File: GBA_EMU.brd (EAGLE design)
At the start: 130.7 x 72.9 mm, 78 parts, among them IC1 MEGA16U2, J2 AUDIO-JACK2SMD, Q1 MOSFET-PCHANNEL, SW1 LEFT, SW2 RIGHT, SW3 PWR_SWITCH, SW4 R2, SW5 L2, U1 RPI-ZERO, U2 FT230X, U3 MCP1642B-ADJ, U4 LM4875, U5 V_REG_LDOSMD2, U6 MIC7221, U7 AZV321

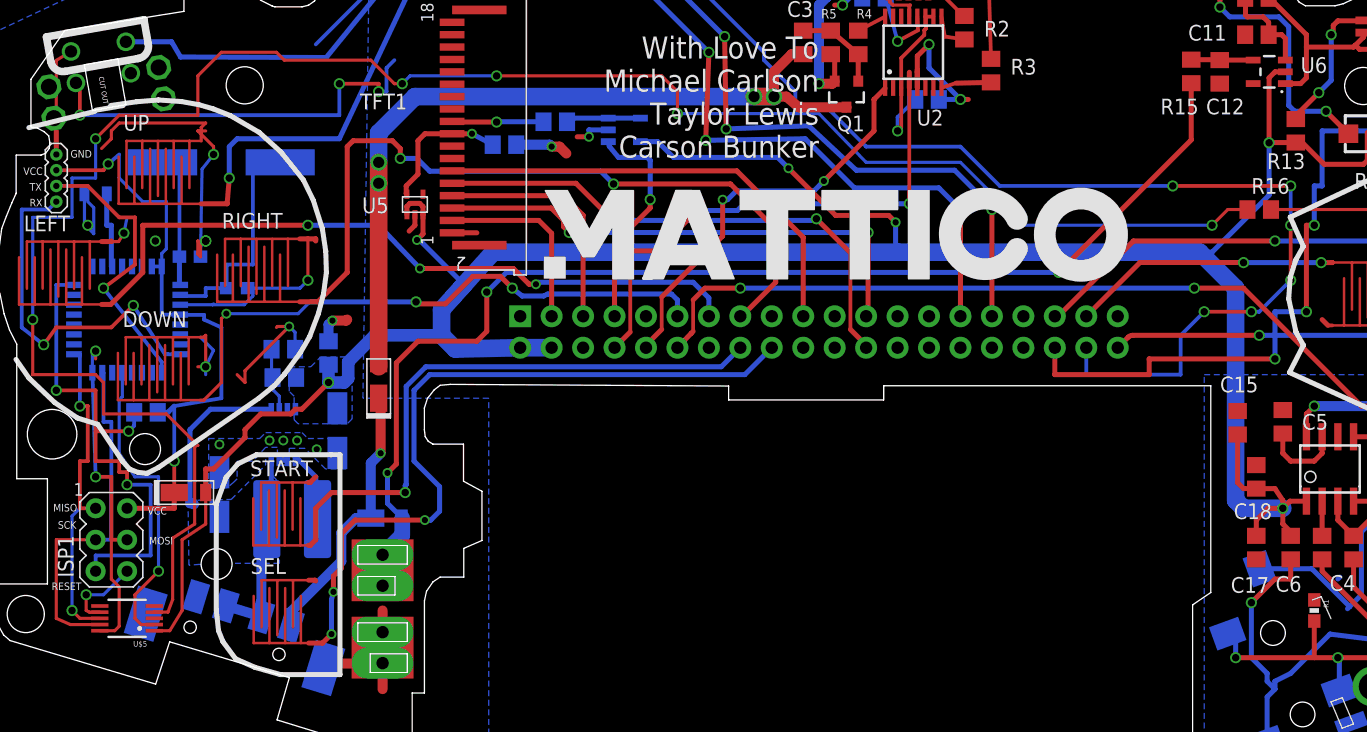
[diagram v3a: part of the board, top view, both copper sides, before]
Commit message: added soureable switch
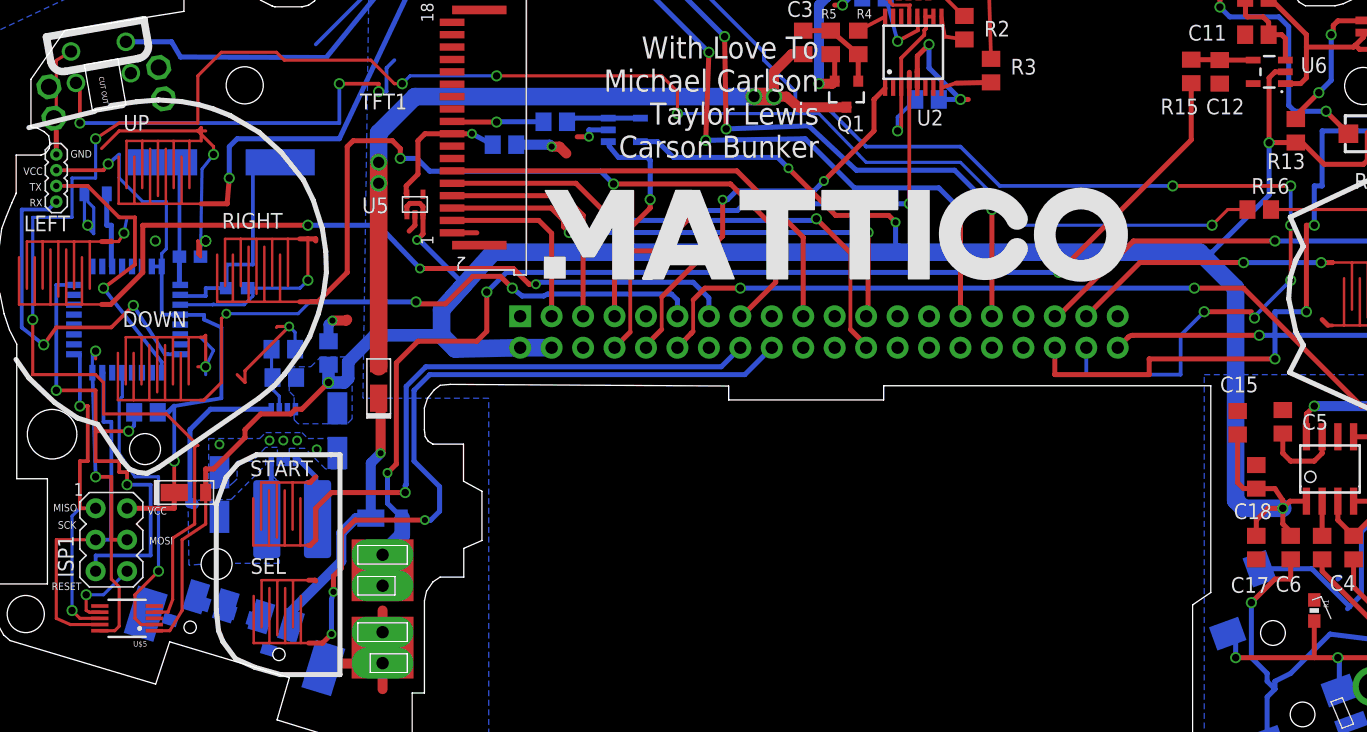
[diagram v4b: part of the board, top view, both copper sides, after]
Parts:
- added SW6: GBA_PWR_SWITCHJSX, custom:JSX08001SAQNL_SWITCH
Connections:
- new net N$13: SW3.1
- net 0.8128: no longer SW3.COM1, SW3.COM2
- net N$18: no longer SW3.1
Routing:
- net 0.8128: track 30.2 -> 22.2 mm
- net L2_BUMP: track 155.6 -> 157.5 mm
- net GND: track 178.2 -> 176.8 mm
- net N$18: track 22.1 -> 21.0 mm
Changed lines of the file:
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@@
 <attribute name="PROD_ID" value="RES-07871" x="127.635" y="23.495" size="1.778" layer="27" rot="R270" display="off"/>
 </element>
+<element name="SW6" library="custom" package="JSX08001SAQNL_SWITCH" value="GBA_PWR_SWITCHJSX" x="43.18" y="20.32" rot="MR17"/>
 </elements>
 <signals>
@@
 <contactref element="U$5" pad="7"/>
 <wire x1="37.737625" y1="61.42204375" x2="37.737625" y2="62.502625" width="0.254" layer="1"/>
-<wire x1="37.737625" y1="62.502625" x2="38.1" y2="62.865" width="0.254" layer="1"/>
-<wire x1="38.1" y1="62.865" x2="31.115" y2="62.865" width="0.254" layer="1"/>
+<wire x1="37.737625" y1="62.502625" x2="37.465" y2="62.23" width="0.254" layer="1"/>
+<wire x1="37.465" y1="62.23" x2="31.115" y2="62.23" width="0.254" layer="1"/>
 <wire x1="26.035" y1="62.23" x2="26.035" y2="67.92616875" width="0.254" layer="1"/>
 <wire x1="26.035" y1="67.92616875" x2="27.221940625" y2="68.644228125" width="0.254" layer="1"/>
@@
 <wire x1="38.735" y1="60.96" x2="37.465" y2="62.23" width="0.254" layer="1"/>
 <wire x1="37.465" y1="62.23" x2="38.1" y2="62.23" width="0.254" layer="1"/>
-<wire x1="29.69269375" y1="60.80769375" x2="30.48" y2="61.595" width="0.254" layer="1"/>
-<wire x1="30.48" y1="61.595" x2="30.48" y2="62.23" width="0.254" layer="1"/>
-<wire x1="30.48" y1="62.23" x2="31.115" y2="62.865" width="0.254" layer="1"/>
+<wire x1="29.69269375" y1="60.80769375" x2="31.115" y2="62.23" width="0.254" layer="1"/>
 <wire x1="29.55" y1="23.36" x2="28.71" y2="23.36" width="0.254" layer="1"/>
 <wire x1="28.71" y1="23.36" x2="28.448" y2="23.495" width="0.254" layer="1"/>
@@
 <wire x1="123.8262125" y1="12.886290625" x2="123.8262125" y2="16.5112125" width="0.4064" layer="16"/>
 <wire x1="123.8262125" y1="16.5112125" x2="124.46" y2="17.145" width="0.4064" layer="16"/>
-<wire x1="40.64" y1="42.545" x2="38.1" y2="42.545" width="0" layer="19" extent="1-16"/>
+<wire x1="42.61191875" y1="25.943271875" x2="31.75" y2="26.67" width="0" layer="19" extent="1-1"/>
+<wire x1="38.1" y1="42.545" x2="40.64" y2="42.545" width="0" layer="19" extent="1-16"/>
 <wire x1="96.52" y1="69.215" x2="94.925" y2="71.455" width="0" layer="19" extent="1-16"/>
-<wire x1="31.75" y1="26.67" x2="42.61191875" y2="25.943271875" width="0" layer="19" extent="1-1"/>
+<wire x1="128.740265625" y1="46.519734375" x2="125.095" y2="39.685" width="0" layer="19" extent="1-1"/>
 </signal>
 <signal name="TXD">
@@
 <wire x1="36.83" y1="38.1" x2="36.83" y2="32.146875" width="0.4064" layer="16"/>
 <wire x1="43.395625" y1="30.76125" x2="43.395625" y2="28.835625" width="0.8128" layer="16"/>
-<contactref element="SW3" pad="COM2"/>
-<contactref element="SW3" pad="COM1"/>
-<wire x1="42.59605625" y1="22.99866875" x2="42.59605625" y2="28.03605625" width="0.8128" layer="16"/>
 <wire x1="42.59605625" y1="28.03605625" x2="43.395625" y2="28.835625" width="0.8128" layer="16"/>
-<wire x1="42.59605625" y1="22.99866875" x2="39.727140625" y2="23.875784375" width="0.8128" layer="16"/>
 </signal>
 <signal name="N$20">
@@
 <wire x1="50.244375" y1="30.95625" x2="49.05375" y2="29.765625" width="0.8128" layer="16"/>
 <wire x1="49.05375" y1="29.765625" x2="49.05375" y2="27.46375" width="0.8128" layer="16"/>
-<contactref element="SW3" pad="1"/>
-<wire x1="44.986815625" y1="22.267740625" x2="44.986815625" y2="23.396815625" width="0.8128" layer="16"/>
 <wire x1="44.986815625" y1="23.396815625" x2="49.05375" y2="27.46375" width="0.8128" layer="16"/>
 </signal>
@@
 <wire x1="43.815" y1="68.58" x2="39.37" y2="68.58" width="0.254" layer="1"/>
 <wire x1="39.37" y1="68.58" x2="37.465" y2="66.675" width="0.254" layer="1"/>
-<wire x1="37.465" y1="66.675" x2="37.465" y2="63.5" width="0.254" layer="1"/>
-<wire x1="37.465" y1="63.5" x2="31.115" y2="63.5" width="0.254" layer="1"/>
-<wire x1="31.115" y1="63.5" x2="29.21" y2="61.595" width="0.254" layer="1"/>
+<wire x1="37.465" y1="66.675" x2="37.465" y2="62.865" width="0.254" layer="1"/>
+<wire x1="37.465" y1="62.865" x2="31.115" y2="62.865" width="0.254" layer="1"/>
+<wire x1="31.115" y1="62.865" x2="29.21" y2="61.595" width="0.254" layer="1"/>
 <via x="29.21" y="61.595" extent="1-16" drill="0.6"/>
 <wire x1="29.21" y1="61.595" x2="29.21" y2="58.42" width="0.254" layer="16"/>
@@
 <contactref element="U1" pad="38"/>
 <wire x1="27.6227125" y1="66.110503125" x2="27.94" y2="66.110503125" width="0.3048" layer="1"/>
-<wire x1="27.94" y1="66.110503125" x2="27.94" y2="63.5" width="0.3048" layer="1"/>
-<via x="27.94" y="63.5" extent="1-16" drill="0.6" shape="square"/>
-<wire x1="27.94" y1="63.5" x2="48.895" y2="63.5" width="0.3048" layer="16"/>
-<wire x1="48.895" y1="63.5" x2="48.895" y2="66.04" width="0.3048" layer="16"/>
+<wire x1="27.94" y1="66.110503125" x2="27.94" y2="62.865" width="0.3048" layer="1"/>
+<via x="27.94" y="62.865" extent="1-16" drill="0.6" shape="square"/>
+<wire x1="27.94" y1="62.865" x2="48.895" y2="62.865" width="0.3048" layer="16"/>
+<wire x1="48.895" y1="62.865" x2="48.895" y2="66.04" width="0.3048" layer="16"/>
 <via x="48.895" y="66.04" extent="1-16" drill="0.6" shape="square"/>
 <wire x1="48.895" y1="66.04" x2="52.07" y2="66.04" width="0.3048" layer="1"/>
@@
 <wire x1="116.84" y1="42.545" x2="116.84" y2="45.72" width="0.3048" layer="16"/>
 <wire x1="116.84" y1="45.72" x2="118.745" y2="47.625" width="0.3048" layer="16"/>
-<via x="118.745" y="47.625" extent="1-16" drill="0.6" shape="square"/>
-<wire x1="118.745" y1="47.625" x2="122.555" y2="47.625" width="0.3048" layer="1"/>
-<via x="122.555" y="47.625" extent="1-16" drill="0.6" shape="square"/>
-<wire x1="122.555" y1="47.625" x2="123.19" y2="47.625" width="0.3048" layer="16"/>
-<wire x1="123.19" y1="47.625" x2="125.73" y2="50.165" width="0.3048" layer="16"/>
+<wire x1="122.809" y1="47.244" x2="125.73" y2="50.165" width="0.3048" layer="16"/>
 <via x="125.73" y="50.165" extent="1-16" drill="0.6" shape="square"/>
 <wire x1="125.73" y1="50.165" x2="125.73" y2="54.61" width="0.3048" layer="1"/>
@@
 <wire x1="52.07" y1="75.565" x2="52.07" y2="74.295" width="0.3048" layer="16"/>
 <wire x1="52.07" y1="74.295" x2="46.99" y2="69.215" width="0.3048" layer="16"/>
+<via x="118.745" y="47.625" extent="1-16" drill="0.6"/>
+<wire x1="118.745" y1="47.625" x2="122.555" y2="47.625" width="0.4064" layer="1"/>
+<wire x1="122.555" y1="47.625" x2="122.555" y2="47.371" width="0.3048" layer="1"/>
+<wire x1="122.555" y1="47.371" x2="122.809" y2="47.117" width="0.3048" layer="1"/>
+<via x="122.809" y="47.117" extent="1-16" drill="0.6"/>
+<wire x1="122.809" y1="47.117" x2="122.809" y2="47.244" width="0.3048" layer="16"/>
 <wire x1="48.895" y1="66.04" x2="46.99" y2="69.215" width="0" layer="19" extent="1-16"/>
 </signal>
@@
 <wire x1="127.635" y1="22.645" x2="127.635" y2="19.685" width="0.4064" layer="1"/>
 </signal>
+<signal name="N$13">
+<contactref element="SW3" pad="1"/>
+</signal>
 </signals>

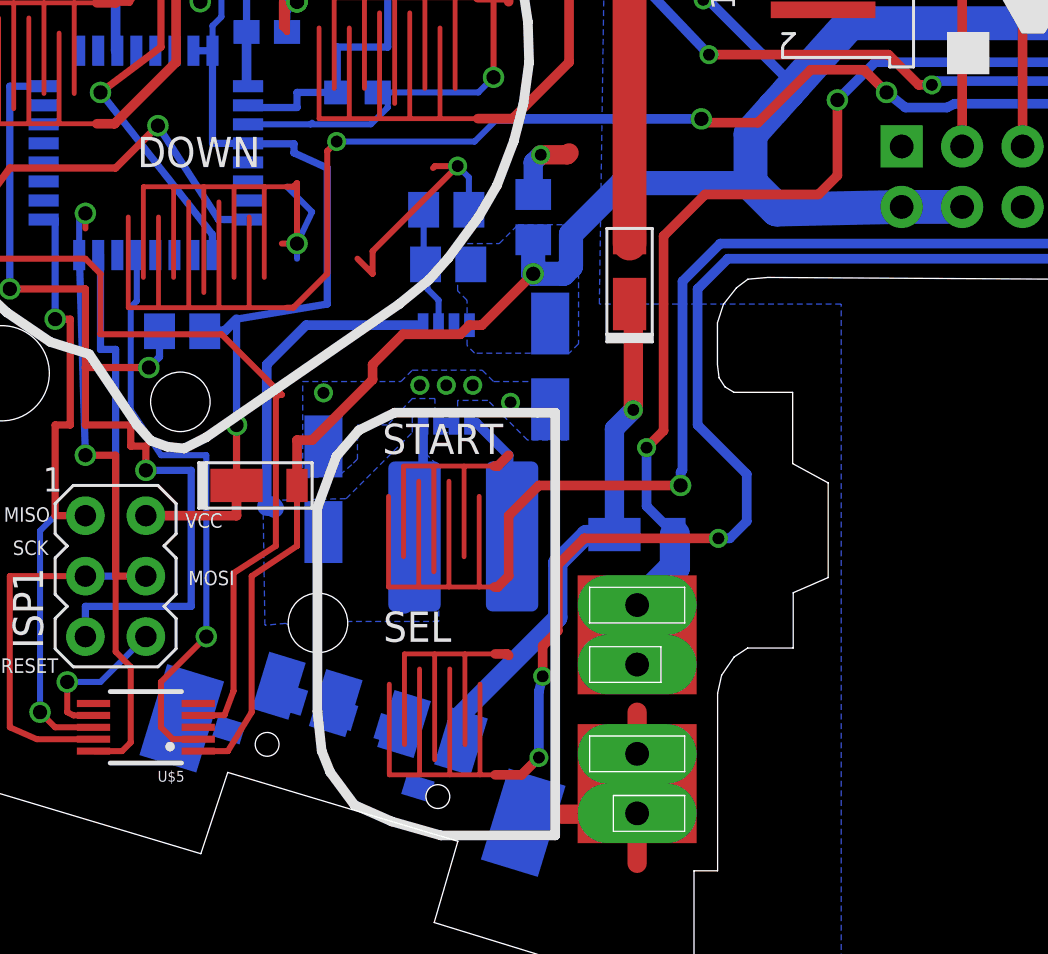
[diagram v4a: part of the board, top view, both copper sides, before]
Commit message: added a sourceable switch
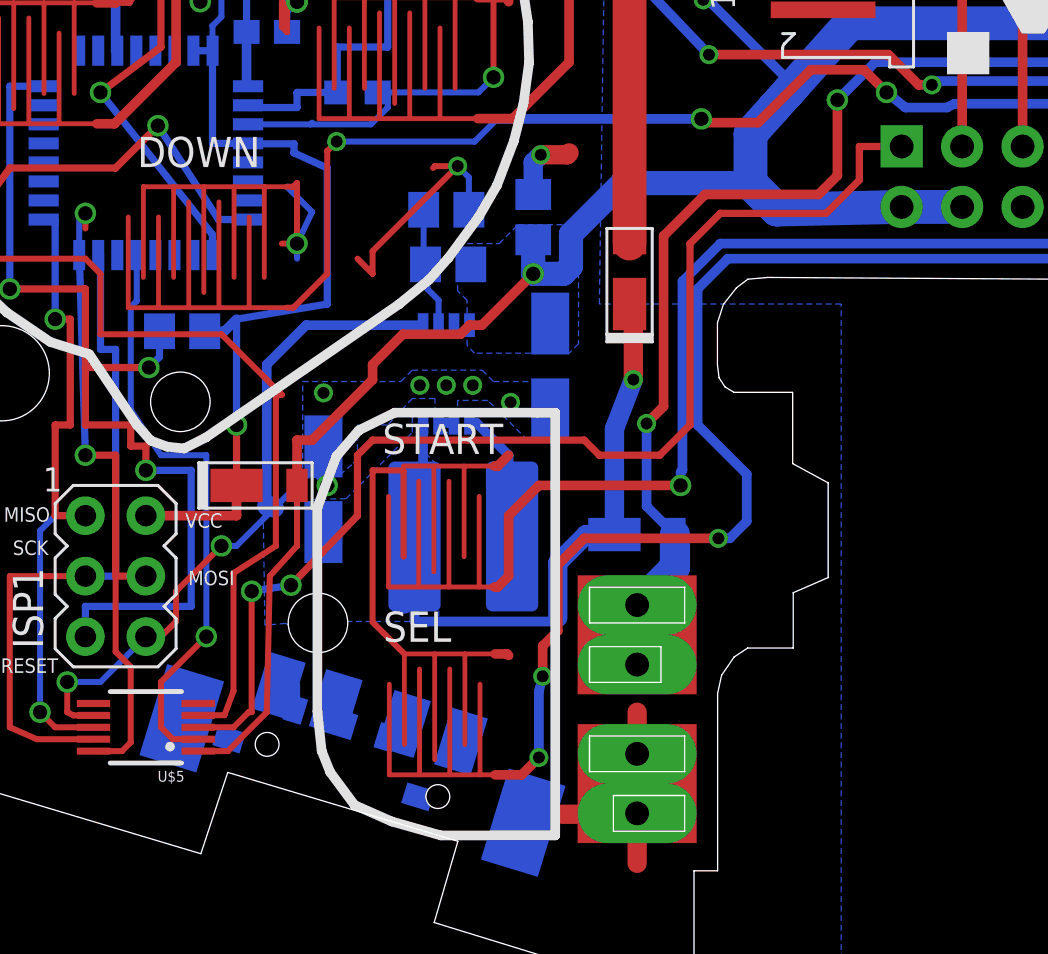
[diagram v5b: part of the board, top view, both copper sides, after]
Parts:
- SW3: value PWR_SWITCH -> ORG_SW
- SW6: value GBA_PWR_SWITCHJSX -> (none)
- moved SW6 0.38 mm to (43.2, 19.9)
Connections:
- removed net N$13: SW3.1
- removed net N$18: D1.2, D2.2
- new net PWR_SW_CM: SW3.COM1, SW3.COM2, SW6.P$5
- new net PWR_SW_NC: SW3.1, SW6.P$3
- new net PWR_SW_NO: SW3.2, SW6.P$4
- net 0.8128: now also D1.2, D2.2
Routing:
- net 3.3V: track 0.00 -> 49.9 mm, vias 0 -> 2
- net 0.8128: track 22.2 -> 49.3 mm, vias 0 -> 1
- net GND: track 176.8 -> 202.7 mm, vias 24 -> 26
- net N$18: track 21.0 -> 0.00 mm, vias 1 -> 0
- net PWR_SW_NO: track 0.00 -> 1.69 mm
- net PWR_SW_CM: track 0.00 -> 1.23 mm

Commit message: still need to route power
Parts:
- removed SW3: ORG_SW, GBA:PWR_SWITCH
- added C22: 0.1uF, SparkFun-Capacitors:0603-CAP
- added D5, D6, D7: IN4001, diode:SOD-123_MINI-SMA
- added R18: 100k, SparkFun-Resistors:0603-RES
- added R19, R20: 10K, SparkFun-Resistors:0603-RES
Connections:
- removed net PWR_SW_CM: SW3.COM1, SW3.COM2, SW6.P$5
- removed net PWR_SW_NC: SW3.1, SW6.P$3
- removed net PWR_SW_NO: SW3.2, SW6.P$4
- new net N$13: D5.A, D7.C
- new net N$18: IC1.7, R19.1
- new net N$30: C22.2, IC1.6, R20.1
- new net N$31: D5.C, R20.2
- new net PWR_EN: D6.C, R18.2, R19.2, U3.1
- new net PWR_SW: D6.A, D7.A, SW6.P$4
- net 0.8128: now also SW6.P$5; no longer U3.1
- net GND: now also C22.1, R18.1
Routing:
- net GND: track 202.7 -> 323.9 mm, vias 26 -> 31
- net PWR_EN: track 0.00 -> 32.4 mm
- net PWR_SW: track 0.00 -> 13.9 mm
- net L2_BUMP: track 157.5 -> 150.0 mm
- net DAC_OUT: track 163.0 -> 168.0 mm
- net N$30: track 0.00 -> 3.86 mm
- net N$18: track 0.00 -> 2.92 mm
- net 5V: track 248.2 -> 250.7 mm, vias 7 -> 8
- net 0.8128: track 49.3 -> 51.5 mm, vias 1 -> 2
- net PWR_SW_NO: track 1.69 -> 0.00 mm
- net PWR_SW_CM: track 1.23 -> 0.00 mm

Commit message: fixed erc
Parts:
- moved D7 54.3 mm to (57.4, 30.7), turned to 270 degrees
- moved D5 22.3 mm to (48.3, 41.9), flipped to the top
- moved R18 1.14 mm to (41.3, 40.8)
- moved R19 0.69 mm to (39.4, 43.1)
- moved R20 0.38 mm to (39.4, 44.7)
- moved C22 0.13 mm to (39.4, 46.5)
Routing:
- net N$13: track 0.00 -> 18.9 mm, vias 0 -> 2
- net PWR_SW: track 13.9 -> 30.8 mm, vias 0 -> 1
- net N$31: track 0.00 -> 8.65 mm, vias 0 -> 1
- net GND: track 323.9 -> 325.9 mm
- net N$18: track 2.92 -> 3.86 mm
- net N$4: track 13.3 -> 14.2 mm
- net N$30: track 3.86 -> 4.69 mm
- net PWR_EN: track 32.4 -> 31.7 mm
- net AVR_VCC: track 51.2 -> 50.6 mm

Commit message: last fixes
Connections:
- removed net N$30: C22.2, IC1.6, R20.1
- new net PWR_SW_STATE: C22.2, IC1.6, R20.1, U1.37
- net B_BTN: now also U1.33; no longer U1.37
- net GND: now also IC1.28
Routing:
- net PWR_SW_STATE: track 0.00 -> 124.1 mm, vias 0 -> 6
- net B_BTN: track 21.7 -> 27.5 mm, vias 2 -> 4
- net N$30: track 4.69 -> 0.00 mm
- net R2_BUMP: track 60.5 -> 63.8 mm
- net N$2: track 66.3 -> 69.1 mm
- net GND: track 325.9 -> 324.7 mm, vias 31 -> 32
- net 5V: track 251.2 -> 250.4 mm
- net SELECT: track 60.1 -> 60.2 mm, vias 3 -> 1
